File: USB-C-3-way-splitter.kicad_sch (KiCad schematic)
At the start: 31 parts, among them J1 USB_C_Receptacle_USB2.0, J2 Conn_01x05_Socket, J3 Conn_01x05_Socket, J4 Conn_01x05_Socket, U1 LM393, U2 SiP32509

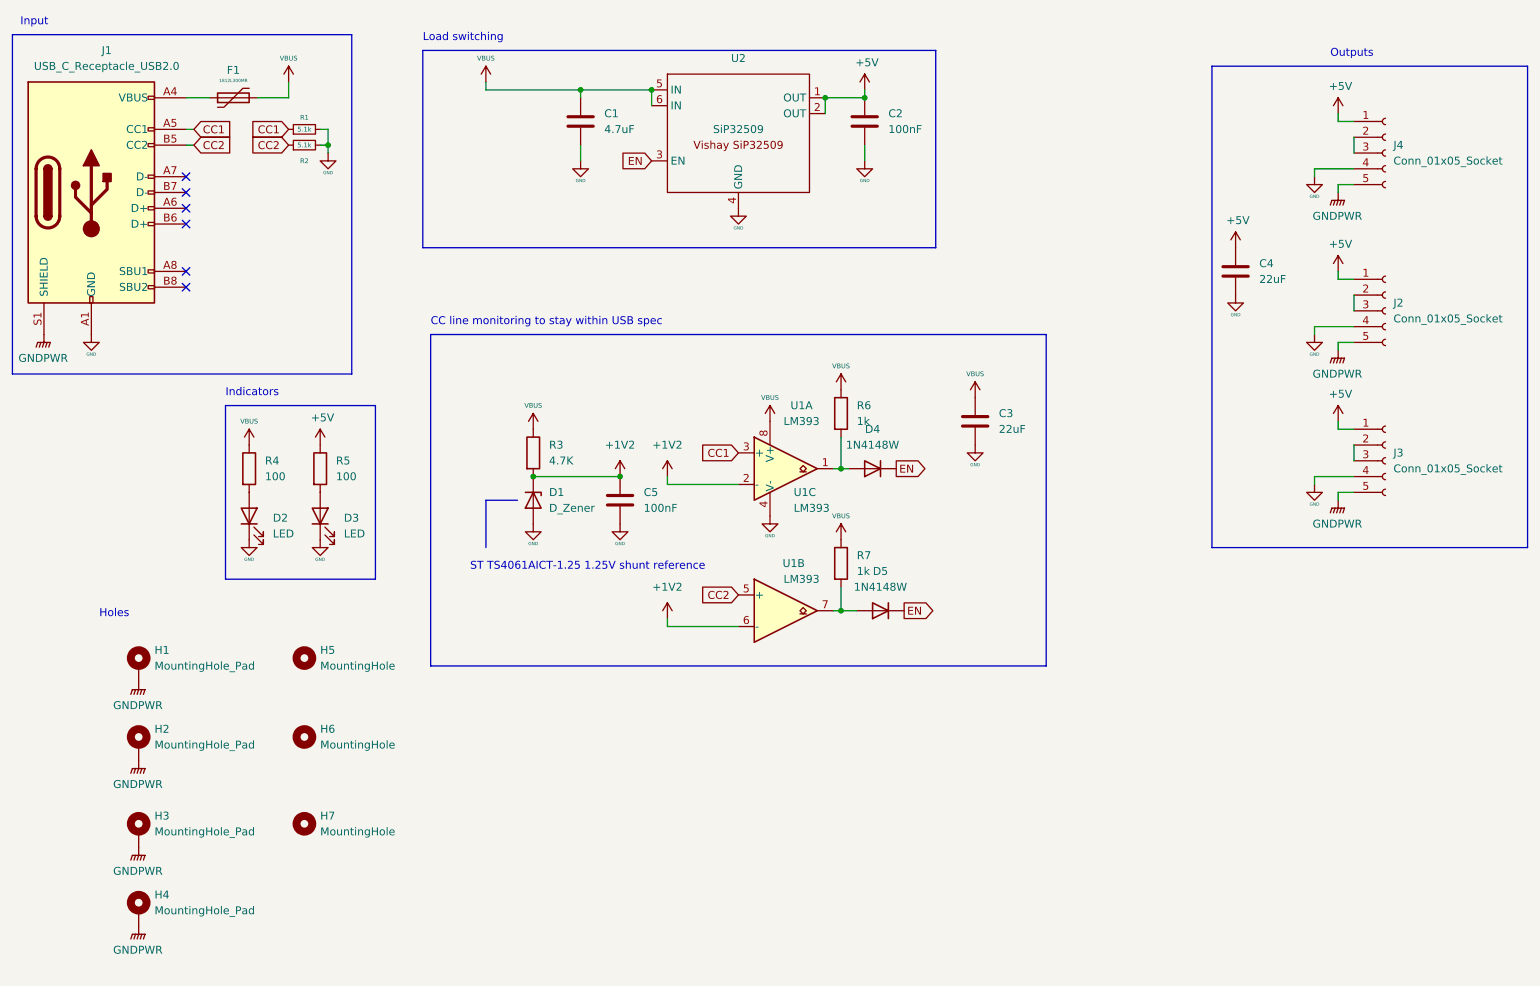
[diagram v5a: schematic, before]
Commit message: Added pulldown to EN, added test points
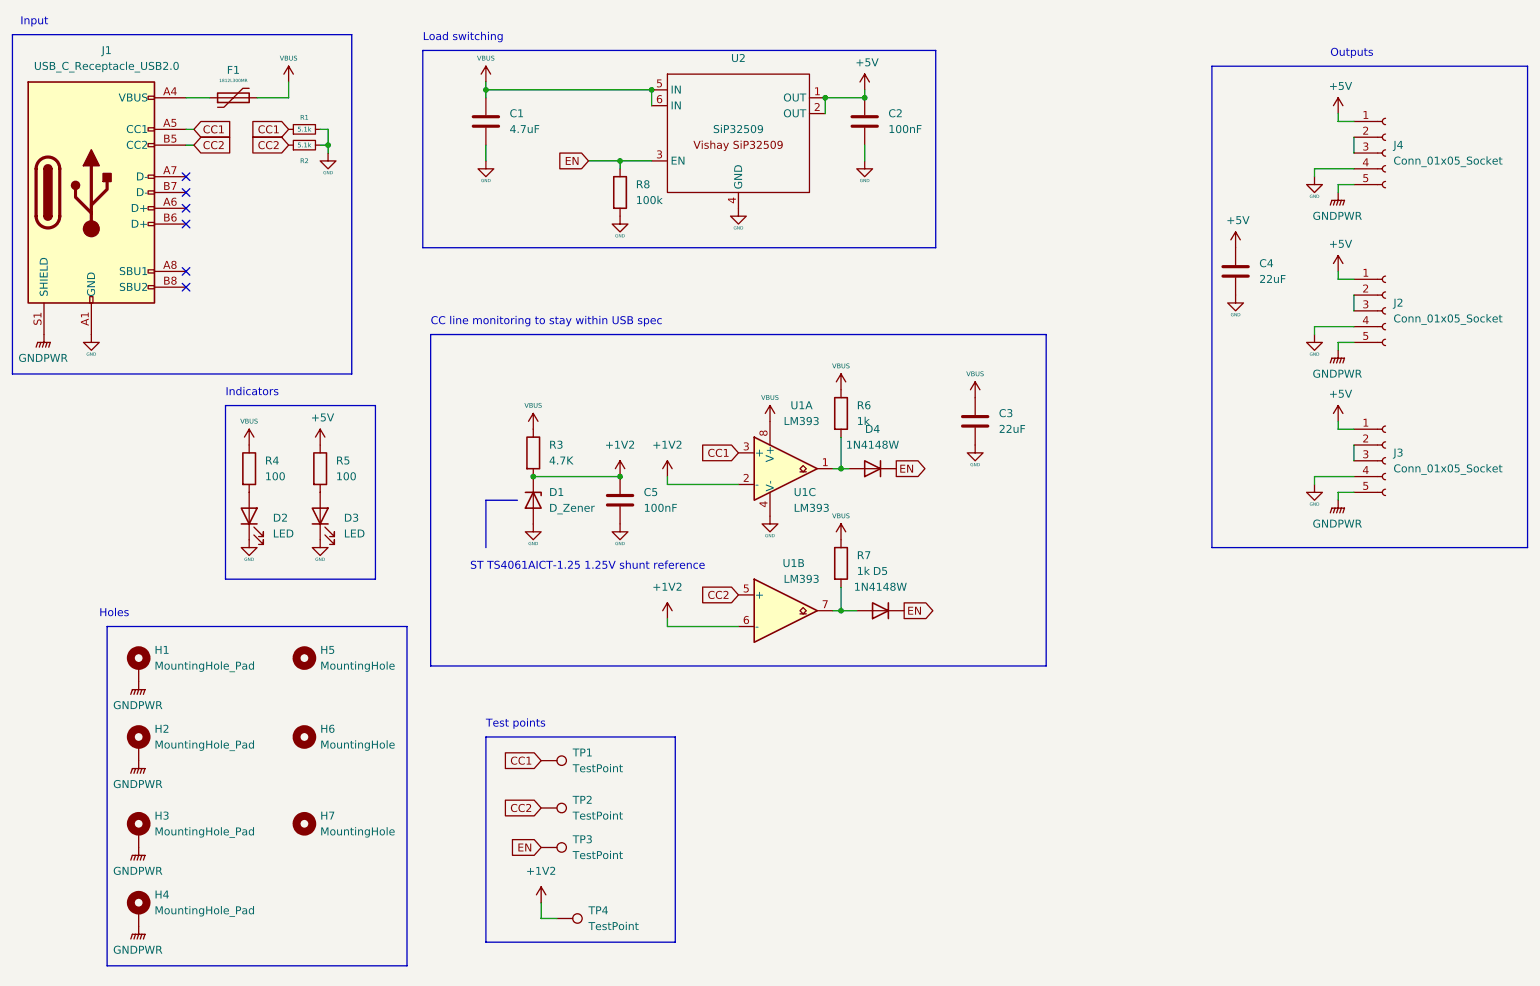
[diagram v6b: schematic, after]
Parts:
- added R8: 100k, Resistor_SMD:R_0805_2012Metric_Pad1.20x1.40mm_HandSolder, symbol Device:R
- added TP1, TP2, TP3, TP4: TestPoint, TestPoint:TestPoint_Pad_D2.5mm, symbol Connector:TestPoint
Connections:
- net +1V2: now also TP4.1
- net CC1: now also TP1.1
- net CC2: now also TP2.1
- net EN: now also R8.1, TP3.1
- net GND: now also R8.2
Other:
- note added: "Test points"
- moved on the sheet: C1

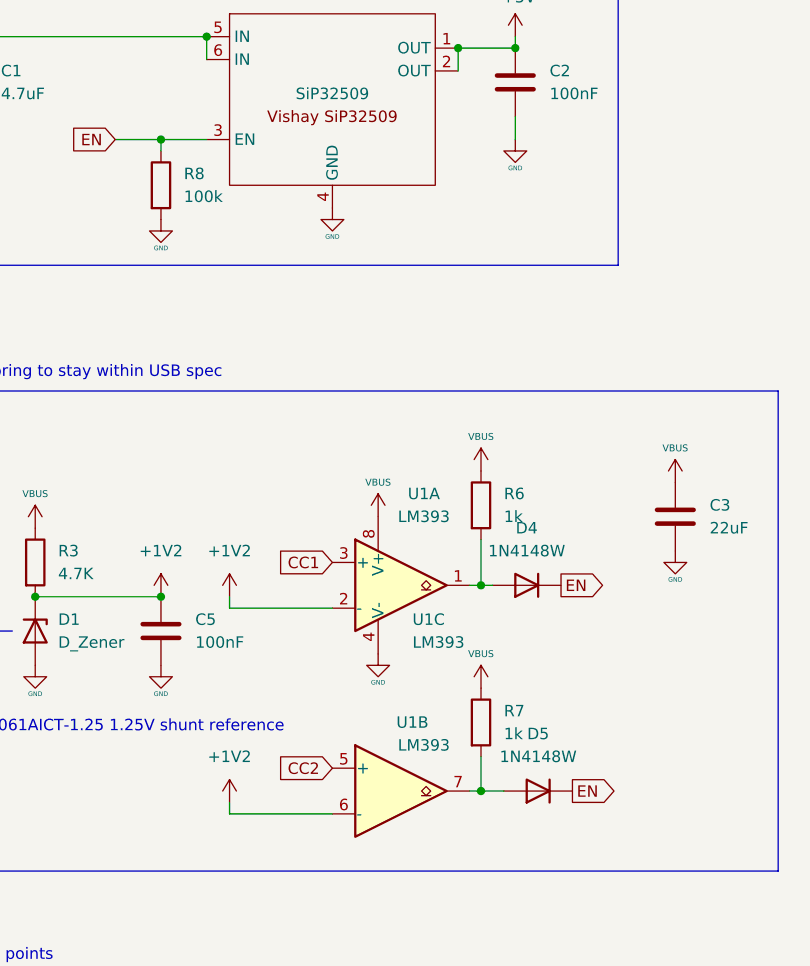
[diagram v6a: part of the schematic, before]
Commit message: Removed unnecessary diodes and resistor
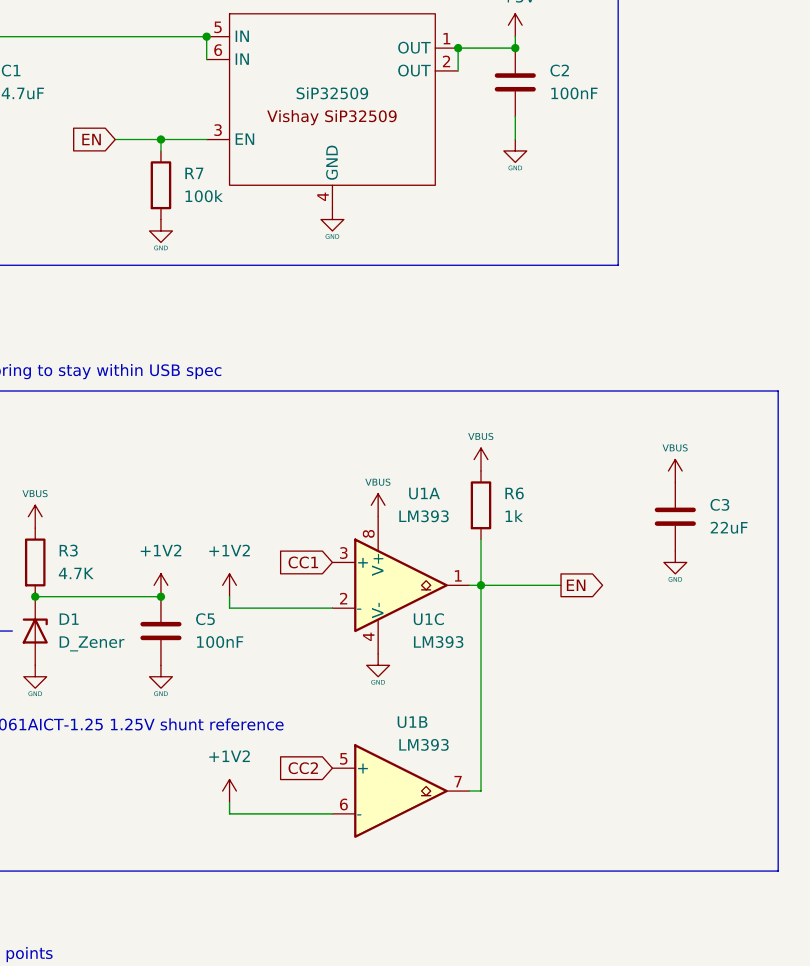
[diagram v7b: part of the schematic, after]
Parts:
- removed D4, D5: 1N4148W, Diode_SMD:D_SOD-123, symbol Diode:1N4148W
- removed R7: 1k, Resistor_SMD:R_0805_2012Metric_Pad1.20x1.40mm_HandSolder, symbol Device:R
- renumbered R8 to R7
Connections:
- net EN: now also R6.2, U1.1, U1.7
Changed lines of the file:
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@@
   (junction (at 151.13 90.17) (diameter 0) (color 0 0 0 0)
-  )
-  (junction (at 151.13 113.03) (diameter 0) (color 0 0 0 0)
   )
   (junction (at 120.65 29.21) (diameter 0) (color 0 0 0 0)
@@
     (stroke (width 0) (type default))
   )
+  (wire (pts (xy 151.13 90.17) (xy 151.13 113.03))
+    (stroke (width 0) (type default))
+  )
   (wire (pts (xy 154.94 30.48) (xy 148.59 30.48))
     (stroke (width 0) (type default))
@@
     (stroke (width 0) (type default))
   )
-  (wire (pts (xy 151.13 109.22) (xy 151.13 113.03))
-    (stroke (width 0) (type default))
-  )
   (wire (pts (xy 233.68 69.85) (xy 231.14 69.85))
     (stroke (width 0) (type default))
@@
     (stroke (width 0) (type solid))
   )
-  (wire (pts (xy 151.13 113.03) (xy 153.67 113.03))
-    (stroke (width 0) (type default))
-  )
   (polyline (pts (xy 166.37 54.61) (xy 83.82 54.61))
     (stroke (width 0) (type default))
@@
     (stroke (width 0) (type default))
   )
-  (wire (pts (xy 151.13 90.17) (xy 152.4 90.17))
+  (wire (pts (xy 151.13 90.17) (xy 160.02 90.17))
     (stroke (width 0) (type default))
   )
@@
     (property "Intersheetrefs" "${INTERSHEET_REFS}" (at 55.4002 38.1 0)
       (effects (font (size 1.27 1.27)) (justify right) hide)
-    )
-  )
-  (global_label "EN" (shape output) (at 161.29 113.03 0) (fields_autoplaced)
-    (effects (font (size 1.27 1.27)) (justify left))
-    (property "Intersheetrefs" "${INTERSHEET_REFS}" (at 166.8498 113.03 0)
-      (effects (font (size 1.27 1.27)) (justify left) hide)
     )
   )
@@
     )
   )
-  (symbol (lib_id "Diode:1N4148W") (at 156.21 90.17 180) (unit 1)
-    (in_bom yes) (on_board yes) (dnp no) (fields_autoplaced)
-    (property "Reference" "D4" (at 156.21 83.82 0)
-      (effects (font (size 1.27 1.27)))
-    )
-    (property "Value" "1N4148W" (at 156.21 86.36 0)
-      (effects (font (size 1.27 1.27)))
-    )
-    (property "Footprint" "Diode_SMD:D_SOD-123" (at 156.21 85.725 0)
-      (effects (font (size 1.27 1.27)) hide)
-    )
-    (property "Datasheet" "https://www.vishay.com/docs/85748/1n4148w.pdf" (at 156.21 90.17 0)
-      (effects (font (size 1.27 1.27)) hide)
-    )
-    (property "Sim.Device" "D" (at 156.21 90.17 0)
-      (effects (font (size 1.27 1.27)) hide)
-    )
-    (property "Sim.Pins" "1=K 2=A" (at 156.21 90.17 0)
-      (effects (font (size 1.27 1.27)) hide)
-    )
-    (pin "2")
-    (pin "1")
-    (instances
-      (project "USB-C-3-way-splitter"
-        (path "/49b03f2e-4a93-4c4e-8d95-13775b5bcebc"
-          (reference "D4") (unit 1)
-        )
-      )
-    )
-  )
   (symbol (lib_id "power:+5V") (at 214.63 54.61 0) (unit 1)
     (in_bom yes) (on_board yes) (dnp no)
@@
         (path "/49b03f2e-4a93-4c4e-8d95-13775b5bcebc"
           (reference "#PWR028") (unit 1)
-        )
-      )
-    )
-  )
-  (symbol (lib_id "Device:R") (at 151.13 105.41 0) (unit 1)
-    (in_bom yes) (on_board yes) (dnp no) (fields_autoplaced)
-    (property "Reference" "R7" (at 153.67 104.14 0)
-      (effects (font (size 1.27 1.27)) (justify left))
-    )
-    (property "Value" "1k" (at 153.67 106.68 0)
-      (effects (font (size 1.27 1.27)) (justify left))
-    )
-    (property "Footprint" "Resistor_SMD:R_0805_2012Metric_Pad1.20x1.40mm_HandSolder" (at 149.352 105.41 90)
-      (effects (font (size 1.27 1.27)) hide)
-    )
-    (property "Datasheet" "~" (at 151.13 105.41 0)
-      (effects (font (size 1.27 1.27)) hide)
-    )
-    (pin "2")
-    (pin "1")
-    (instances
-      (project "USB-C-3-way-splitter"
-        (path "/49b03f2e-4a93-4c4e-8d95-13775b5bcebc"
-          (reference "R7") (unit 1)
         )
       )
@@
         (path "/49b03f2e-4a93-4c4e-8d95-13775b5bcebc"
           (reference "C3") (unit 1)
-        )
-      )
-    )
-  )
-  (symbol (lib_id "power:VBUS") (at 151.13 101.6 0) (unit 1)
-    (in_bom yes) (on_board yes) (dnp no)
-    (property "Reference" "#PWR026" (at 151.13 105.41 0)
-      (effects (font (size 1.27 1.27)) hide)
-    )
-    (property "Value" "VBUS" (at 151.13 97.79 0)
-      (effects (font (size 0.762 0.762)))
-    )
-    (property "Footprint" "" (at 151.13 101.6 0)
-      (effects (font (size 1.27 1.27)) hide)
-    )
-    (property "Datasheet" "" (at 151.13 101.6 0)
-      (effects (font (size 1.27 1.27)) hide)
-    )
-    (pin "1")
-    (instances
-      (project "USB-C-3-way-splitter"
-        (path "/49b03f2e-4a93-4c4e-8d95-13775b5bcebc"
-          (reference "#PWR026") (unit 1)
         )
       )
@@
   (symbol (lib_id "Device:R") (at 115.57 45.72 0) (unit 1)
     (in_bom yes) (on_board yes) (dnp no) (fields_autoplaced)
-    (property "Reference" "R8" (at 118.11 44.45 0)
+    (property "Reference" "R7" (at 118.11 44.45 0)
       (effects (font (size 1.27 1.27)) (justify left))
     )
@@
       (project "USB-C-3-way-splitter"
         (path "/49b03f2e-4a93-4c4e-8d95-13775b5bcebc"
-          (reference "R8") (unit 1)
+          (reference "R7") (unit 1)
         )
       )
@@
         )
       )
-    )
-  )
-  (symbol (lib_id "Diode:1N4148W") (at 157.48 113.03 180) (unit 1)
-    (in_bom yes) (on_board yes) (dnp no) (fields_autoplaced)
-    (property "Reference" "D5" (at 157.48 106.68 0)
-      (effects (font (size 1.27 1.27)))
-    )
-    (property "Value" "1N4148W" (at 157.48 109.22 0)
-      (effects (font (size 1.27 1.27)))
-    )
-    (property "Footprint" "Diode_SMD:D_SOD-123" (at 157.48 108.585 0)
-      (effects (font (size 1.27 1.27)) hide)
-    )
-    (property "Datasheet" "https://www.vishay.com/docs/85748/1n4148w.pdf" (at 157.48 113.03 0)
-      (effects (font (size 1.27 1.27)) hide)
-    )
-    (property "Sim.Device" "D" (at 157.48 113.03 0)
-      (effects (font (size 1.27 1.27)) hide)
-    )
-    (property "Sim.Pins" "1=K 2=A" (at 157.48 113.03 0)
-      (effects (font (size 1.27 1.27)) hide)
-    )
-    (pin "2")
-    (pin "1")
-    (instances
-      (project "USB-C-3-way-splitter"
-        (path "/49b03f2e-4a93-4c4e-8d95-13775b5bcebc"
-          (reference "D5") (unit 1)
-        )
-      )
